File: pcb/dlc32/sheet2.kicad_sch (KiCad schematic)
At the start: 29 parts, among them IC2 74HCT14, J10 CHILLER SSR PWR, J11 EXHAUST, J12 EXT1, J13 COM2, J14 DLC32:J18, J15 INT PWR, J4 CHILLER SWITCH, J5 CHILLER SSR, J6 AIR VALVE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

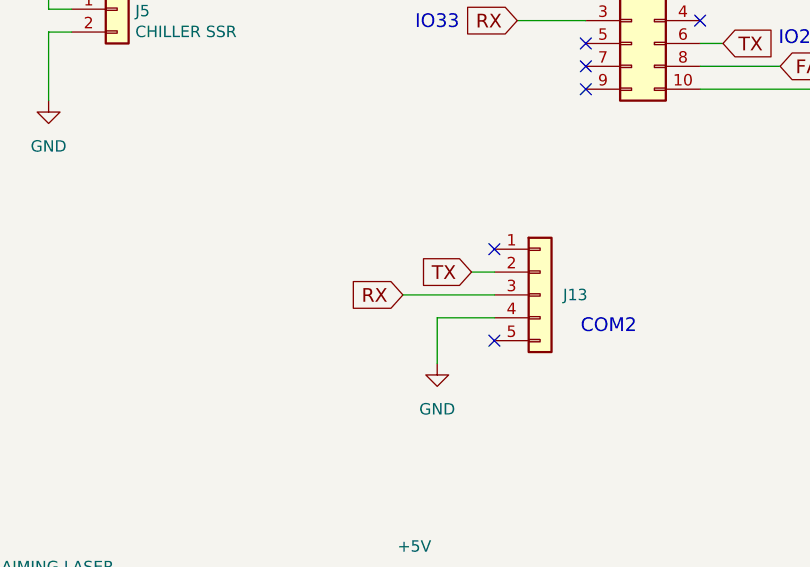
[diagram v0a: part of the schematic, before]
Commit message: Swap RX and TX.
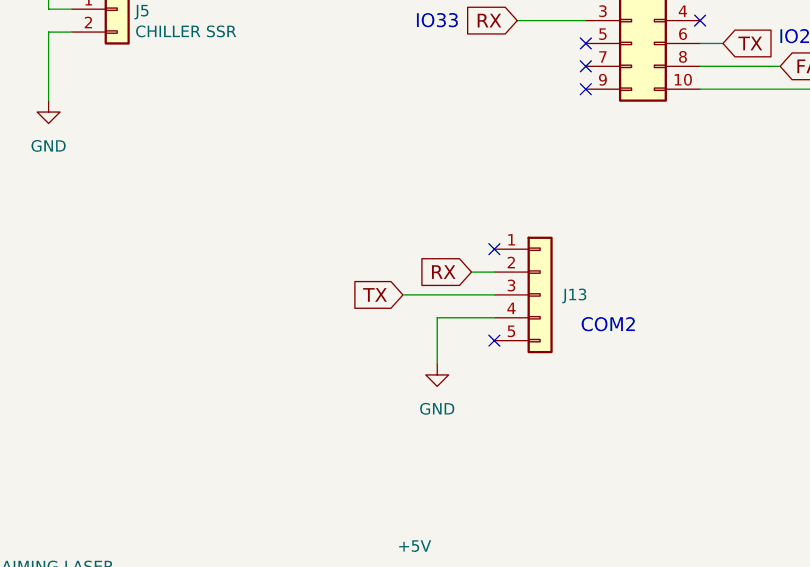
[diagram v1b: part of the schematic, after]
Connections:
- net RX: now also J13.2 (Pin_2); no longer J13.3 (Pin_3)
- net TX: now also J13.3 (Pin_3); no longer J13.2 (Pin_2)
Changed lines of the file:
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@@
 	(global_label "RX"
 		(shape input)
-		(at 133.35 130.81 180)
+		(at 140.97 128.27 180)
 		(fields_autoplaced yes)
 		(effects
@@
 		)
 		(property "Intersheetrefs" "${INTERSHEET_REFS}"
-			(at 126.6786 130.81 0)
+			(at 134.2986 128.27 0)
 			(effects
 				(font
@@
 	(global_label "TX"
 		(shape input)
-		(at 140.97 128.27 180)
+		(at 133.35 130.81 180)
 		(fields_autoplaced yes)
 		(effects
@@
 		)
 		(property "Intersheetrefs" "${INTERSHEET_REFS}"
-			(at 134.6615 128.27 0)
+			(at 127.0415 130.81 0)
 			(effects
 				(font

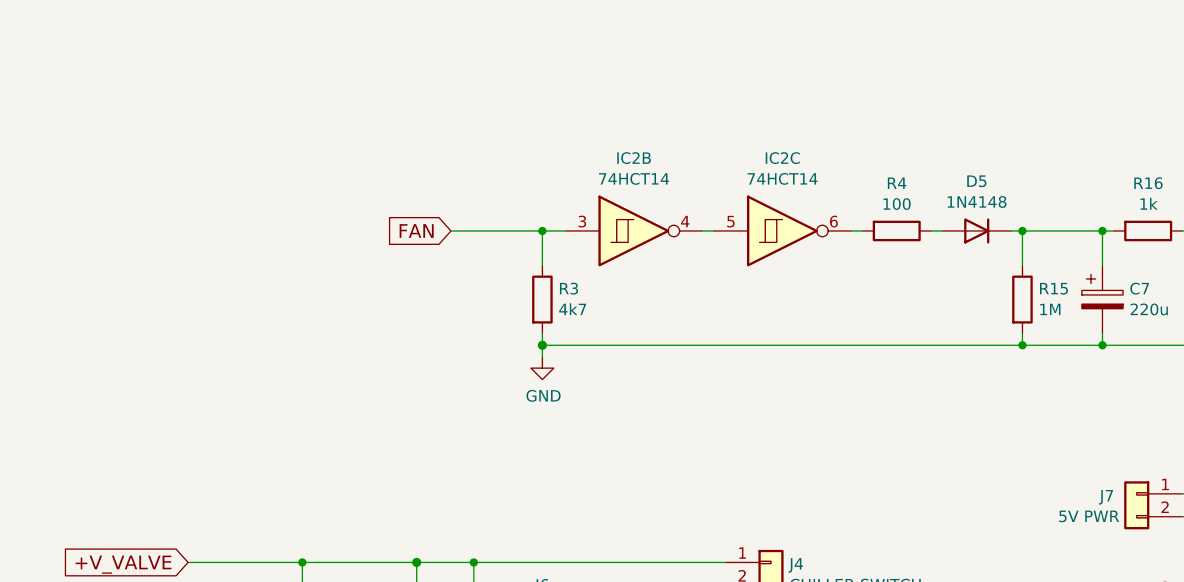
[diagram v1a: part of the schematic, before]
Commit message: Update laser connector, prevent fan activation on startup.
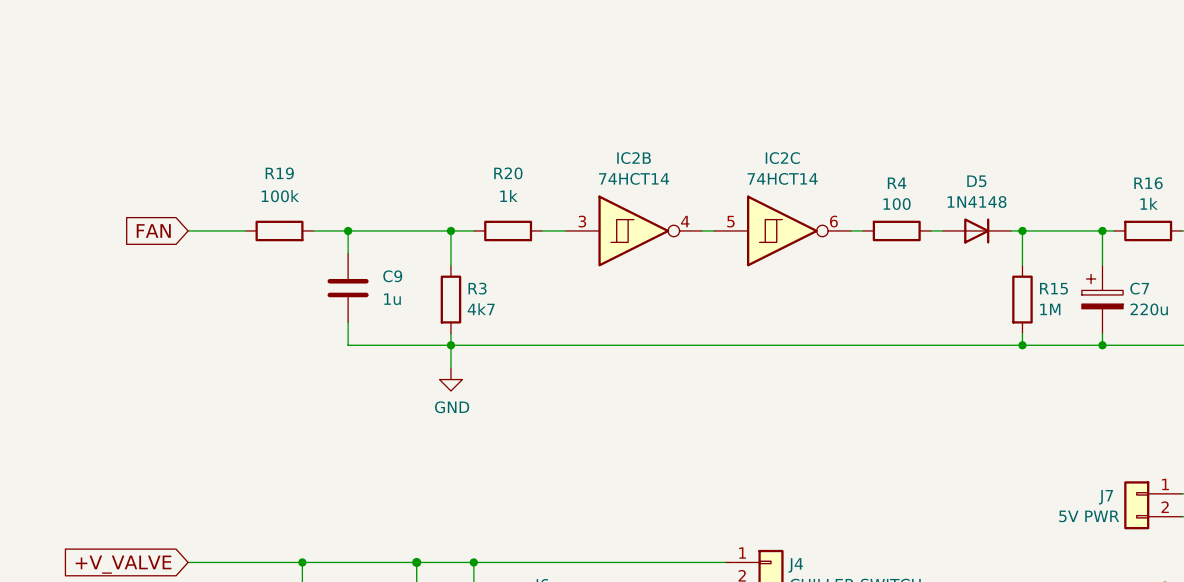
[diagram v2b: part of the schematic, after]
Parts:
- added C9: 1u, symbol Device:C
- added R19: 100k, symbol Device:R
- added R20: 1k, symbol Device:R
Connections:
- net FAN: now also R19.1; no longer IC2.3, R3.1
- net GND: now also C9.2
- new net: C9.1, R19.2, R20.1, R3.1
- new net: IC2.3, R20.2
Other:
- moved on the sheet: R3

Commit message: Add support for dual endstops.
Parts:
- C9: footprint (none) -> Capacitor_SMD:C_0603_1608Metric
- IC2: footprint Package_SO:SOIC-14_3.9x8.7mm_P1.27mm -> PCM_Package_SO_AKL:SOIC-14_3.9x8.7mm_P1.27mm
- R19, R20: footprint (none) -> PCM_Resistor_SMD_AKL:R_0603_1608Metric
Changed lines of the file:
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@@
 			)
 		)
-		(property "Footprint" "Package_SO:SOIC-14_3.9x8.7mm_P1.27mm"
+		(property "Footprint" "PCM_Package_SO_AKL:SOIC-14_3.9x8.7mm_P1.27mm"
 			(at 156.21 50.8 0)
 			(effects
@@
 			)
 		)
-		(property "Footprint" ""
+		(property "Footprint" "PCM_Resistor_SMD_AKL:R_0603_1608Metric"
 			(at 72.39 52.578 90)
 			(effects
@@
 			)
 		)
-		(property "Footprint" "Package_SO:SOIC-14_3.9x8.7mm_P1.27mm"
+		(property "Footprint" "PCM_Package_SO_AKL:SOIC-14_3.9x8.7mm_P1.27mm"
 			(at 86.36 50.8 0)
 			(effects
@@
 			)
 		)
-		(property "Footprint" "Package_SO:SOIC-14_3.9x8.7mm_P1.27mm"
+		(property "Footprint" "PCM_Package_SO_AKL:SOIC-14_3.9x8.7mm_P1.27mm"
 			(at 102.87 50.8 0)
 			(effects
@@
 			)
 		)
-		(property "Footprint" ""
+		(property "Footprint" "Capacitor_SMD:C_0603_1608Metric"
 			(at 55.5752 60.96 0)
 			(effects
@@
 			)
 		)
-		(property "Footprint" ""
+		(property "Footprint" "PCM_Resistor_SMD_AKL:R_0603_1608Metric"
 			(at 46.99 52.578 90)
 			(effects
@@
 			)
 		)
-		(property "Footprint" "Package_SO:SOIC-14_3.9x8.7mm_P1.27mm"
+		(property "Footprint" "PCM_Package_SO_AKL:SOIC-14_3.9x8.7mm_P1.27mm"
 			(at 172.72 50.8 0)
 			(effects
